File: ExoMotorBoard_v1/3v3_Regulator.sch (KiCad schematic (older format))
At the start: 4 parts, among them U1 MIC5219-3_3YM5-TR

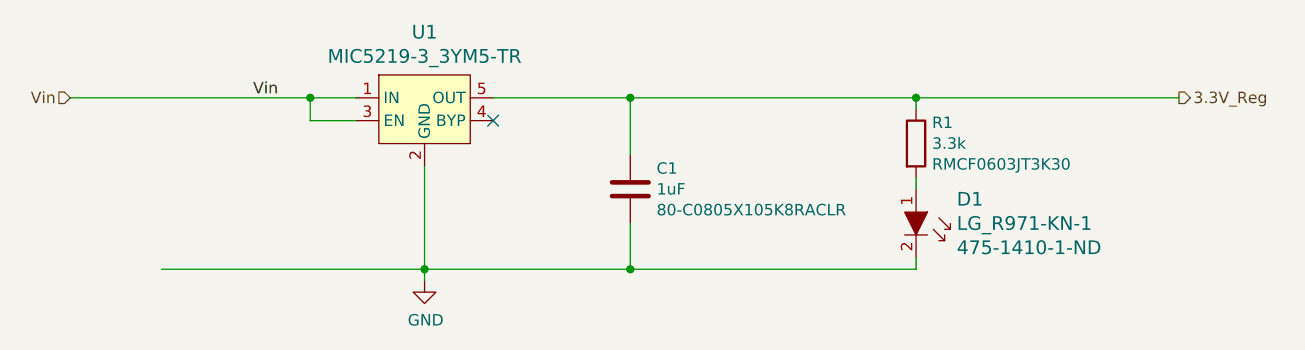
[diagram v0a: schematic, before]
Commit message: MCU connection updated
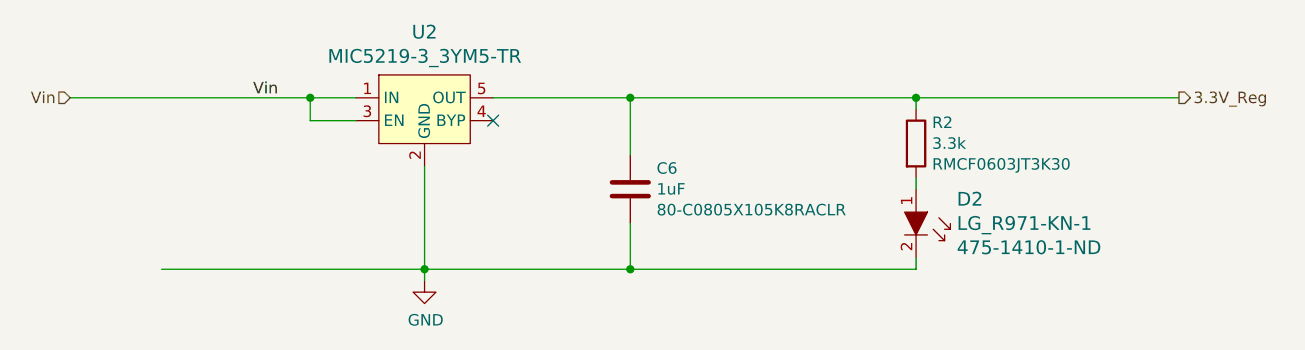
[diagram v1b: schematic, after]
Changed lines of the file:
@@
 AR Path="/610DEFD4/610FDBB2/61100636" Ref="U1"  Part="1"
 AR Path="/610DEFD4/6110D176/61100636" Ref="U2"  Part="1"
-F 0 "U1" H 4400 2287 60  0000 C CNN
+F 0 "U2" H 4400 2287 60  0000 C CNN
 F 1 "MIC5219-3_3YM5-TR" H 4400 2181 60  0000 C CNN
 F 2 "digikey-footprints:SOT-753" H 4600 2200 60  0001 L CNN
@@
 AR Path="/610DEFD4/610FDBB2/6110063D" Ref="C1"  Part="1"
 AR Path="/610DEFD4/6110D176/6110063D" Ref="C6"  Part="1"
-F 0 "C1" H 5415 2491 50  0000 L CNN
+F 0 "C6" H 5415 2491 50  0000 L CNN
 F 1 "1uF" H 5415 2400 50  0000 L CNN
 F 2 "Capacitor_SMD:C_0805_2012Metric_Pad1.18x1.45mm_HandSolder" H 5338 2250 50  0001 C CNN
@@
 AR Path="/610DEFD4/610FDBB2/61100643" Ref="#PWR0101"  Part="1"
 AR Path="/610DEFD4/6110D176/61100643" Ref="#PWR0103"  Part="1"
-F 0 "#PWR0101" H 4400 2550 50  0001 C CNN
+F 0 "#PWR0103" H 4400 2550 50  0001 C CNN
 F 1 "GND" H 4405 2627 50  0000 C CNN
 F 2 "" H 4400 2800 50  0001 C CNN
@@
 AR Path="/610DEFD4/610FDBB2/6110064A" Ref="R1"  Part="1"
 AR Path="/610DEFD4/6110D176/6110064A" Ref="R2"  Part="1"
-F 0 "R1" H 6620 2291 50  0000 L CNN
+F 0 "R2" H 6620 2291 50  0000 L CNN
 F 1 "3.3k" H 6620 2200 50  0000 L CNN
 F 2 "Resistor_SMD:R_0603_1608Metric_Pad0.98x0.95mm_HandSolder" V 6480 2200 50  0001 C CNN
@@
 AR Path="/610DEFD4/610FDBB2/61100687" Ref="D1"  Part="1"
 AR Path="/610DEFD4/6110D176/61100687" Ref="D2"  Part="1"
-F 0 "D1" V 6394 2778 60  0000 L CNN
+F 0 "D2" V 6394 2778 60  0000 L CNN
 F 1 "LG_R971-KN-1" V 6500 2778 60  0000 L CNN
 F 2 "digikey-footprints:0805" H 6750 2800 60  0001 L CNN
